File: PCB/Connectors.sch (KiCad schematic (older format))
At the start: 18 parts

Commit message: Switch 3.3V analog circuitry to low noise supply, fix pin classifications on some parts, swap 9V connector for 10V
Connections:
- net labels added: +10V
- net labels removed: +9V
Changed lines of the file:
@@
 Wire Wire Line
 	6300 4550 6200 4550
-$Comp
-L power:+9V #PWR?
-U 1 1 5DEFE9A9
-P 6200 4550
-F 0 "#PWR?" H 6200 4400 50  0001 C CNN
-F 1 "+9V" H 6215 4723 50  0000 C CNN
-F 2 "" H 6200 4550 50  0001 C CNN
-F 3 "" H 6200 4550 50  0001 C CNN
-	1    6200 4550
-	1    0    0    -1
-$EndComp
 Text GLabel 4800 6250 0    50   Input ~ 0
 FPGA-CS
@@
 Wire Wire Line
 	3550 2000 3650 2000
+$Comp
+L power:+10V #PWR?
+U 1 1 5E281EB9
+P 6200 4550
+F 0 "#PWR?" H 6200 4400 50  0001 C CNN
+F 1 "+10V" H 6215 4723 50  0000 C CNN
+F 2 "" H 6200 4550 50  0001 C CNN
+F 3 "" H 6200 4550 50  0001 C CNN
+	1    6200 4550
+	1    0    0    -1
+$EndComp
 $EndSCHEMATC

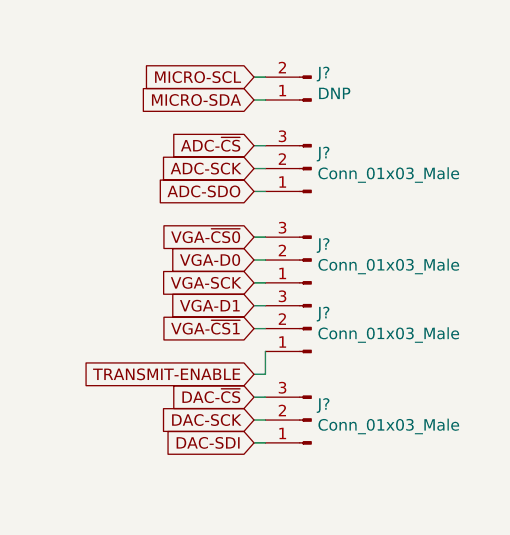
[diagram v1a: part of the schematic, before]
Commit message: Add missing footprints
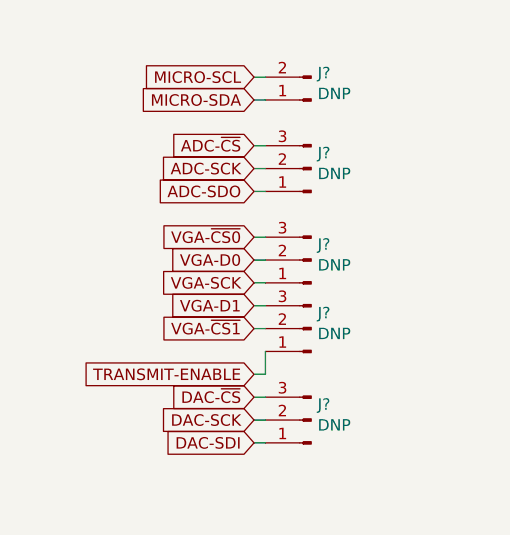
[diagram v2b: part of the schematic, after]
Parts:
- H? (x2): footprint (none) -> Mounting_Holes:MountingHole_4mm_Pad_Via
- J? (x4): value Conn_01x03_Male -> DNP; footprint (none) -> Pin_Headers:Pin_Header_Straight_1x03_Pitch2.54mm
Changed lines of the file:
@@
 P 9050 4900
 F 0 "J?" H 9022 4832 50  0000 R CNN
-F 1 "Conn_01x03_Male" H 9022 4923 50  0000 R CNN
-F 2 "" H 9050 4900 50  0001 C CNN
+F 1 "DNP" H 9022 4923 50  0000 R CNN
+F 2 "Pin_Headers:Pin_Header_Straight_1x03_Pitch2.54mm" H 9050 4900 50  0001 C CNN
 F 3 "~" H 9050 4900 50  0001 C CNN
 	1    9050 4900
@@
 P 9050 5300
 F 0 "J?" H 9022 5232 50  0000 R CNN
-F 1 "Conn_01x03_Male" H 9022 5323 50  0000 R CNN
-F 2 "" H 9050 5300 50  0001 C CNN
+F 1 "DNP" H 9022 5323 50  0000 R CNN
+F 2 "Pin_Headers:Pin_Header_Straight_1x03_Pitch2.54mm" H 9050 5300 50  0001 C CNN
 F 3 "~" H 9050 5300 50  0001 C CNN
 	1    9050 5300
@@
 P 9050 5600
 F 0 "J?" H 9022 5532 50  0000 R CNN
-F 1 "Conn_01x03_Male" H 9022 5623 50  0000 R CNN
-F 2 "" H 9050 5600 50  0001 C CNN
+F 1 "DNP" H 9022 5623 50  0000 R CNN
+F 2 "Pin_Headers:Pin_Header_Straight_1x03_Pitch2.54mm" H 9050 5600 50  0001 C CNN
 F 3 "~" H 9050 5600 50  0001 C CNN
 	1    9050 5600
@@
 P 9050 6000
 F 0 "J?" H 9022 5932 50  0000 R CNN
-F 1 "Conn_01x03_Male" H 9022 6023 50  0000 R CNN
-F 2 "" H 9050 6000 50  0001 C CNN
+F 1 "DNP" H 9022 6023 50  0000 R CNN
+F 2 "Pin_Headers:Pin_Header_Straight_1x03_Pitch2.54mm" H 9050 6000 50  0001 C CNN
 F 3 "~" H 9050 6000 50  0001 C CNN
 	1    9050 6000
@@
 F 0 "H?" V 3704 2400 50  0000 L CNN
 F 1 "MountingHole_Pad" V 3795 2400 50  0000 L CNN
-F 2 "" H 3750 2250 50  0001 C CNN
+F 2 "Mounting_Holes:MountingHole_4mm_Pad_Via" H 3750 2250 50  0001 C CNN
 F 3 "~" H 3750 2250 50  0001 C CNN
 	1    3750 2250
@@
 F 0 "H?" V 3704 2150 50  0000 L CNN
 F 1 "MountingHole_Pad" V 3795 2150 50  0000 L CNN
-F 2 "" H 3750 2000 50  0001 C CNN
+F 2 "Mounting_Holes:MountingHole_4mm_Pad_Via" H 3750 2000 50  0001 C CNN
 F 3 "~" H 3750 2000 50  0001 C CNN
 	1    3750 2000

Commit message: Annotate schematic, simplify transmit circuit, shuffle receive opamp stages, reorder buttons so they match net names, reorder connectors to simplify routing, begin arranging parts on PCB
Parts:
- gave numbers to parts that had none: 18
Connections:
- net ADC-SCK: now also J8.1 (Pin_1); no longer J8.2 (Pin_2)
- net ADC-SDO: now also J8.2 (Pin_2); no longer J8.1 (Pin_1)
- net DAC-SCK: now also J15.1 (Pin_1); no longer J15.2 (Pin_2)
- net DAC-SDI: now also J15.2 (Pin_2); no longer J15.1 (Pin_1)

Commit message: Begin layout around FPGA and microcontroller, rearrange some connections to FPGA and microcontroller, change groupings of optional debug pins
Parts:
- removed J10, J11, J15: DNP, Pin_Headers:Pin_Header_Straight_1x03_Pitch2.54mm, symbol Connector:Conn_01x03_Male
- removed J12: PH1-08-UA, Pin_Headers:Pin_Header_Straight_1x08_Pitch2.54mm, symbol Connector:Conn_01x08_Male
- added J10: DNP, Pin_Headers:Pin_Header_Straight_1x05_Pitch2.54mm, symbol Connector:Conn_01x05_Male
- added J11: DNP, Pin_Headers:Pin_Header_Straight_2x05_Pitch2.54mm, symbol Connector_Generic:Conn_02x05_Odd_Even
- added J14: DNP, Pin_Headers:Pin_Header_Straight_1x04_Pitch2.54mm, symbol Connector:Conn_01x04_Male
- renumbered J13 to J12, J14 to J13
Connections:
- net +2V5: now also J11.4 (Pin_4)
- net DAC-SCK: now also J14.3 (Pin_3)
- net DAC-SDI: now also J14.2 (Pin_2)
- net DAC-~CS: now also J14.1 (Pin_1)
- net FPGA-TCK: now also J11.1 (Pin_1)
- net FPGA-TDI: now also J11.9 (Pin_9)
- net FPGA-TDO: now also J11.3 (Pin_3)
- net FPGA-TMS: now also J11.5 (Pin_5)
- net GND: now also J11.10 (Pin_10), J11.2 (Pin_2)
- net TRANSMIT-ENABLE: now also J14.4 (Pin_4)
- net VGA-D0: now also J10.2 (Pin_2)
- net VGA-D1: now also J10.5 (Pin_5)
- net VGA-SCK: now also J10.3 (Pin_3)
- net VGA-~CS0: now also J10.1 (Pin_1)
- net VGA-~CS1: now also J10.4 (Pin_4)
- no-connect marks 0 -> 3
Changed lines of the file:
@@
 Wire Wire Line
 	5700 3000 5700 3050
-Text GLabel 2750 5850 0    50   Input ~ 0
+Text GLabel 2500 5950 0    50   Input ~ 0
 FPGA-TDI
-Text GLabel 2750 5650 0    50   Input ~ 0
+Text GLabel 2500 5550 0    50   Input ~ 0
 FPGA-TCK
-Text GLabel 2750 5950 0    50   Input ~ 0
+Text GLabel 2500 5750 0    50   Input ~ 0
 FPGA-TMS
-Text GLabel 2750 6050 0    50   Input ~ 0
+Text GLabel 2500 5650 0    50   Input ~ 0
 FPGA-TDO
 $Comp
@@
 Wire Wire Line
 	2750 4300 2800 4300
-$Comp
-L Connector:Conn_01x08_Male J12
-U 1 1 5DD1A649
-P 3000 5850
-F 0 "J12" H 2972 5824 50  0000 R CNN
-F 1 "PH1-08-UA" H 2972 5733 50  0000 R CNN
-F 2 "Pin_Headers:Pin_Header_Straight_1x08_Pitch2.54mm" H 3000 5850 50  0001 C CNN
-F 3 "https://www.digikey.ca/product-detail/en/adam-tech/PH1-08-UA/2057-PH1-08-UA-ND/9830442" H 3000 5850 50  0001 C CNN
-	1    3000 5850
-	-1   0    0    -1
-$EndComp
 Wire Wire Line
 	2750 4500 2800 4500
@@
 	2050 4100 2800 4100
 Connection ~ 2050 4400
-Wire Wire Line
-	2700 5550 2800 5550
 $Comp
 L power:GND #PWR0194
 U 1 1 5DD3A2BB
-P 2050 6200
-F 0 "#PWR0194" H 2050 5950 50  0001 C CNN
-F 1 "GND" H 2055 6027 50  0000 C CNN
-F 2 "" H 2050 6200 50  0001 C CNN
-F 3 "" H 2050 6200 50  0001 C CNN
-	1    2050 6200
-	1    0    0    -1
-$EndComp
-Wire Wire Line
-	2750 5650 2800 5650
-Wire Wire Line
-	2750 6050 2800 6050
-Wire Wire Line
-	2800 5950 2750 5950
-Wire Wire Line
-	2750 5850 2800 5850
-Wire Wire Line
-	2050 6200 2050 6150
-Wire Wire Line
-	2050 6150 2800 6150
-Wire Wire Line
-	2050 6150 2050 5750
-Wire Wire Line
-	2050 5750 2800 5750
-Connection ~ 2050 6150
+P 3150 6000
+F 0 "#PWR0194" H 3150 5750 50  0001 C CNN
+F 1 "GND" H 3155 5827 50  0000 C CNN
+F 2 "" H 3150 6000 50  0001 C CNN
+F 3 "" H 3150 6000 50  0001 C CNN
+	1    3150 6000
+	1    0    0    -1
+$EndComp
 $Comp
 L Connector:Conn_01x02_Male J2
@@
 L power:+2V5 #PWR0191
 U 1 1 5DDAEE31
-P 2700 5550
-F 0 "#PWR0191" H 2700 5400 50  0001 C CNN
-F 1 "+2V5" H 2715 5723 50  0000 C CNN
-F 2 "" H 2700 5550 50  0001 C CNN
-F 3 "" H 2700 5550 50  0001 C CNN
-	1    2700 5550
+P 3250 5650
+F 0 "#PWR0191" H 3250 5500 50  0001 C CNN
+F 1 "+2V5" H 3265 5823 50  0000 C CNN
+F 2 "" H 3250 5650 50  0001 C CNN
+F 3 "" H 3250 5650 50  0001 C CNN
+	1    3250 5650
 	1    0    0    -1
 $EndComp
@@
 $EndComp
 $Comp
-L Connector:Conn_01x02_Male J14
+L Connector:Conn_01x02_Male J13
 U 1 1 5DED5F02
 P 6500 5950
-F 0 "J14" H 6472 5832 50  0000 R CNN
+F 0 "J13" H 6472 5832 50  0000 R CNN
 F 1 "DNP" H 6472 5923 50  0000 R CNN
 F 2 "Pin_Headers:Pin_Header_Straight_1x02_Pitch2.54mm" H 6500 5950 50  0001 C CNN
@@
 $EndComp
 $Comp
-L Connector:Conn_01x08_Male J13
+L Connector:Conn_01x08_Male J12
 U 1 1 5DEE094B
 P 5050 5850
-F 0 "J13" H 5022 5824 50  0000 R CNN
+F 0 "J12" H 5022 5824 50  0000 R CNN
 F 1 "DNP" H 5022 5733 50  0000 R CNN
 F 2 "Pin_Headers:Pin_Header_Straight_1x08_Pitch2.54mm" H 5050 5850 50  0001 C CNN
@@
 Text GLabel 8800 4900 0    50   Input ~ 0
 ADC-SDO
-Text GLabel 8800 5200 0    50   Input ~ 0
+Text GLabel 8800 5600 0    50   Input ~ 0
 VGA-~CS0
-Text GLabel 8800 5300 0    50   Input ~ 0
+Text GLabel 8800 5500 0    50   Input ~ 0
 VGA-D0
 Text GLabel 8800 5400 0    50   Input ~ 0
 VGA-SCK
-Text GLabel 8800 5500 0    50   Input ~ 0
+Text GLabel 8800 5200 0    50   Input ~ 0
 VGA-D1
-Text GLabel 8800 5600 0    50   Input ~ 0
+Text GLabel 8800 5300 0    50   Input ~ 0
 VGA-~CS1
+Text GLabel 8800 6100 0    50   Input ~ 0
+DAC-~CS
 Text GLabel 8800 5900 0    50   Input ~ 0
-DAC-~CS
-Text GLabel 8800 6100 0    50   Input ~ 0
 DAC-SCK
 Text GLabel 8800 6000 0    50   Input ~ 0
@@
 Wire Wire Line
 	8800 5000 8850 5000
-$Comp
-L Connector:Conn_01x03_Male J10
-U 1 1 5E232910
-P 9050 5300
-F 0 "J10" H 9022 5232 50  0000 R CNN
-F 1 "DNP" H 9022 5323 50  0000 R CNN
-F 2 "Pin_Headers:Pin_Header_Straight_1x03_Pitch2.54mm" H 9050 5300 50  0001 C CNN
-F 3 "~" H 9050 5300 50  0001 C CNN
-	1    9050 5300
-	-1   0    0    1
-$EndComp
 Wire Wire Line
 	8800 5200 8850 5200
@@
 Wire Wire Line
 	8800 5400 8850 5400
-$Comp
-L Connector:Conn_01x03_Male J11
-U 1 1 5E236FC5
-P 9050 5600
-F 0 "J11" H 9022 5532 50  0000 R CNN
-F 1 "DNP" H 9022 5623 50  0000 R CNN
-F 2 "Pin_Headers:Pin_Header_Straight_1x03_Pitch2.54mm" H 9050 5600 50  0001 C CNN
-F 3 "~" H 9050 5600 50  0001 C CNN
-	1    9050 5600
-	-1   0    0    1
-$EndComp
 Wire Wire Line
 	8800 5500 8850 5500
@@
 Wire Wire Line
 	8800 5800 8850 5800
-Wire Wire Line
-	8850 5800 8850 5700
-$Comp
-L Connector:Conn_01x03_Male J15
-U 1 1 5E23BCC1
-P 9050 6000
-F 0 "J15" H 9022 5932 50  0000 R CNN
-F 1 "DNP" H 9022 6023 50  0000 R CNN
-F 2 "Pin_Headers:Pin_Header_Straight_1x03_Pitch2.54mm" H 9050 6000 50  0001 C CNN
-F 3 "~" H 9050 6000 50  0001 C CNN
-	1    9050 6000
-	-1   0    0    1
-$EndComp
 Wire Wire Line
 	8800 5900 8850 5900
@@
 	1    0    0    -1
 $EndComp
+$Comp
+L Connector_Generic:Conn_02x05_Odd_Even J11
+U 1 1 5E09FA0E
+P 2750 5750
+F 0 "J11" H 2800 6167 50  0000 C CNN
+F 1 "DNP" H 2800 6076 50  0000 C CNN
+F 2 "Pin_Headers:Pin_Header_Straight_2x05_Pitch2.54mm" H 2750 5750 50  0001 C CNN
+F 3 "https://www.digikey.ca/product-detail/en/adam-tech/PH2-10-UA/2057-PH2-10-UA-ND/9830654" H 2750 5750 50  0001 C CNN
+	1    2750 5750
+	1    0    0    -1
+$EndComp
+Wire Wire Line
+	2500 5550 2550 5550
+Wire Wire Line
+	2500 5650 2550 5650
+Wire Wire Line
+	2500 5750 2550 5750
+Wire Wire Line
+	2500 5950 2550 5950
+Wire Wire Line
+	3050 5950 3150 5950
+Wire Wire Line
+	3150 5950 3150 6000
+Wire Wire Line
+	3050 5550 3150 5550
+Wire Wire Line
+	3150 5550 3150 5950
+Connection ~ 3150 5950
+Wire Wire Line
+	3050 5650 3250 5650
+NoConn ~ 3050 5750
+NoConn ~ 3050 5850
+NoConn ~ 2550 5850
+$Comp
+L Connector:Conn_01x04_Male J14
+U 1 1 5E5FD68B
+P 9050 6000
+F 0 "J14" H 9022 5882 50  0000 R CNN
+F 1 "DNP" H 9022 5973 50  0000 R CNN
+F 2 "Pin_Headers:Pin_Header_Straight_1x04_Pitch2.54mm" H 9050 6000 50  0001 C CNN
+F 3 "~" H 9050 6000 50  0001 C CNN
+	1    9050 6000
+	-1   0    0    1
+$EndComp
+$Comp
+L Connector:Conn_01x05_Male J10
+U 1 1 5E600171
+P 9050 5400
+F 0 "J10" H 9022 5332 50  0000 R CNN
+F 1 "DNP" H 9022 5423 50  0000 R CNN
+F 2 "Pin_Headers:Pin_Header_Straight_1x05_Pitch2.54mm" H 9050 5400 50  0001 C CNN
+F 3 "~" H 9050 5400 50  0001 C CNN
+	1    9050 5400
+	-1   0    0    1
+$EndComp
 $EndSCHEMATC

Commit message: Remove unnecessary series resistors, rearrange connections on FPGA and microcontroller, rearrange debug pins, layout most of FPGA and microcontroller sections
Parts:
- removed J12, J5: DNP, Pin_Headers:Pin_Header_Straight_1x08_Pitch2.54mm, symbol Connector:Conn_01x08_Male
- added J5: DNP, Pin_Headers:Pin_Header_Straight_1x15_Pitch2.54mm, symbol Connector:Conn_01x15_Male
- renumbered J13 to J12, J14 to J13, R68 to R64
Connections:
- net FPGA-CONF_DONE: now also J5.1 (Pin_1)
- net FPGA-CRC_ERROR: now also J5.3 (Pin_3)
- net FPGA-CS: now also J5.11 (Pin_11)
- net FPGA-DCLK: now also J5.13 (Pin_13)
- net FPGA-DIN: now also J5.14 (Pin_14)
- net FPGA-DOUT: now also J5.12 (Pin_12)
- net FPGA-INIT_DONE: now also J5.2 (Pin_2)
- net FPGA-LINK0: now also J5.4 (Pin_4)
- net FPGA-LINK1: now also J5.5 (Pin_5)
- net FPGA-LINK2: now also J5.6 (Pin_6)
- net FPGA-LINK3: now also J5.7 (Pin_7)
- net FPGA-LINK4: now also J5.8 (Pin_8)
- net FPGA-LINK5: now also J5.9 (Pin_9)
- net FPGA-nCONFIG: now also J5.15 (Pin_15)
- net FPGA-nSTATUS: now also J5.10 (Pin_10)
- net MICRO-SCL: now also J6.1 (Pin_1); no longer J6.2 (Pin_2)
- net MICRO-SDA: now also J6.2 (Pin_2); no longer J6.1 (Pin_1)
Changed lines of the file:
@@
 $EndDescr
 $Comp
-L power:GND #PWR0180
+L power:GND #PWR0179
 U 1 1 5DCE40E5
 P 2750 2200
-F 0 "#PWR0180" H 2750 1950 50  0001 C CNN
+F 0 "#PWR0179" H 2750 1950 50  0001 C CNN
 F 1 "GND" H 2755 2027 50  0000 C CNN
 F 2 "" H 2750 2200 50  0001 C CNN
@@
 $EndComp
 $Comp
-L power:+BATT #PWR0178
+L power:+BATT #PWR0177
 U 1 1 5DCED91D
 P 3000 2000
-F 0 "#PWR0178" H 3000 1850 50  0001 C CNN
+F 0 "#PWR0177" H 3000 1850 50  0001 C CNN
 F 1 "+BATT" H 3015 2173 50  0000 C CNN
 F 2 "" H 3000 2000 50  0001 C CNN
@@
 TRANSDUCER
 $Comp
-L Device:R R68
+L Device:R R64
 U 1 1 5DE80022
 P 5700 2800
-F 0 "R68" H 5770 2846 50  0000 L CNN
+F 0 "R64" H 5770 2846 50  0000 L CNN
 F 1 "10k" H 5770 2755 50  0000 L CNN
 F 2 "Resistors_SMD:R_1206_HandSoldering" V 5630 2800 50  0001 C CNN
@@
 	5700 2550 5700 2650
 $Comp
-L power:GND #PWR0182
+L power:GND #PWR0181
 U 1 1 5DE80E0C
 P 5700 3050
-F 0 "#PWR0182" H 5700 2800 50  0001 C CNN
+F 0 "#PWR0181" H 5700 2800 50  0001 C CNN
 F 1 "GND" H 5705 2877 50  0000 C CNN
 F 2 "" H 5700 3050 50  0001 C CNN
@@
 FPGA-TDO
 $Comp
-L power:+3V3 #PWR0183
+L power:+3V3 #PWR0182
 U 1 1 5DED008E
 P 2700 3900
-F 0 "#PWR0183" H 2700 3750 50  0001 C CNN
+F 0 "#PWR0182" H 2700 3750 50  0001 C CNN
 F 1 "+3V3" H 2715 4073 50  0000 C CNN
 F 2 "" H 2700 3900 50  0001 C CNN
@@
 	2800 4600 2750 4600
 $Comp
-L power:GND #PWR0186
+L power:GND #PWR0185
 U 1 1 5DD2AB1C
 P 2050 4450
-F 0 "#PWR0186" H 2050 4200 50  0001 C CNN
+F 0 "#PWR0185" H 2050 4200 50  0001 C CNN
 F 1 "GND" H 2055 4277 50  0000 C CNN
 F 2 "" H 2050 4450 50  0001 C CNN
@@
 Connection ~ 2050 4400
 $Comp
-L power:GND #PWR0194
+L power:GND #PWR0193
 U 1 1 5DD3A2BB
 P 3150 6000
-F 0 "#PWR0194" H 3150 5750 50  0001 C CNN
+F 0 "#PWR0193" H 3150 5750 50  0001 C CNN
 F 1 "GND" H 3155 5827 50  0000 C CNN
 F 2 "" H 3150 6000 50  0001 C CNN
@@
 	5950 2650 5950 3000
 $Comp
-L power:+2V5 #PWR0191
+L power:+2V5 #PWR0190
 U 1 1 5DDAEE31
 P 3250 5650
-F 0 "#PWR0191" H 3250 5500 50  0001 C CNN
+F 0 "#PWR0190" H 3250 5500 50  0001 C CNN
 F 1 "+2V5" H 3265 5823 50  0000 C CNN
 F 2 "" H 3250 5650 50  0001 C CNN
@@
 	1    0    0    -1
 $EndComp
-$Comp
-L Connector:Conn_01x08_Male J5
-U 1 1 5DF84ABE
-P 5050 4200
-F 0 "J5" H 5022 4174 50  0000 R CNN
-F 1 "DNP" H 5022 4083 50  0000 R CNN
-F 2 "Pin_Headers:Pin_Header_Straight_1x08_Pitch2.54mm" H 5050 4200 50  0001 C CNN
-F 3 "https://www.digikey.ca/product-detail/en/adam-tech/PH1-08-UA/2057-PH1-08-UA-ND/9830442" H 5050 4200 50  0001 C CNN
-	1    5050 4200
-	-1   0    0    -1
-$EndComp
+Text GLabel 4800 5000 0    50   Input ~ 0
+FPGA-DOUT
+Text GLabel 4800 4800 0    50   Input ~ 0
+FPGA-nSTATUS
+Text GLabel 4800 5100 0    50   Input ~ 0
+FPGA-DCLK
+Text GLabel 4800 5200 0    50   Input ~ 0
+FPGA-DIN
+Text GLabel 4800 5300 0    50   Input ~ 0
+FPGA-nCONFIG
 Text GLabel 4800 3900 0    50   Input ~ 0
-FPGA-DOUT
-Text GLabel 4800 4400 0    50   Input ~ 0
-FPGA-nSTATUS
+FPGA-CONF_DONE
 Text GLabel 4800 4000 0    50   Input ~ 0
-FPGA-DCLK
+FPGA-INIT_DONE
 Text GLabel 4800 4100 0    50   Input ~ 0
-FPGA-DIN
-Text GLabel 4800 4500 0    50   Input ~ 0
-FPGA-nCONFIG
-Text GLabel 4800 4200 0    50   Input ~ 0
-FPGA-CONF_DONE
-Text GLabel 4800 4600 0    50   Input ~ 0
-FPGA-INIT_DONE
-Text GLabel 4800 4300 0    50   Input ~ 0
 FPGA-CRC_ERROR
 Wire Wire Line
@@
 $EndComp
 $Comp
-L power:+1V2 #PWR0184
+L power:+1V2 #PWR0183
 U 1 1 5DECE3B1
 P 6200 3900
-F 0 "#PWR0184" H 6200 3750 50  0001 C CNN
+F 0 "#PWR0183" H 6200 3750 50  0001 C CNN
 F 1 "+1V2" H 6215 4073 50  0000 C CNN
 F 2 "" H 6200 3900 50  0001 C CNN
@@
 	6200 3900 6300 3900
 $Comp
-L power:GND #PWR0185
+L power:GND #PWR0184
 U 1 1 5DECF8CC
 P 6200 4000
-F 0 "#PWR0185" H 6200 3750 50  0001 C CNN
+F 0 "#PWR0184" H 6200 3750 50  0001 C CNN
 F 1 "GND" H 6205 3827 50  0000 C CNN
 F 2 "" H 6200 4000 50  0001 C CNN
@@
 	6200 5200 6300 5200
 $Comp
-L power:GND #PWR0190
+L power:GND #PWR0189
 U 1 1 5DED29DD
 P 6200 5300
-F 0 "#PWR0190" H 6200 5050 50  0001 C CNN
+F 0 "#PWR0189" H 6200 5050 50  0001 C CNN
 F 1 "GND" H 6205 5127 50  0000 C CNN
 F 2 "" H 6200 5300 50  0001 C CNN
@@
 	6200 5300 6300 5300
 $Comp
-L power:+12V #PWR0189
+L power:+12V #PWR0188
 U 1 1 5DED51C9
 P 6200 5200
-F 0 "#PWR0189" H 6200 5050 50  0001 C CNN
+F 0 "#PWR0188" H 6200 5050 50  0001 C CNN
 F 1 "+12V" H 6215 5373 50  0000 C CNN
 F 2 "" H 6200 5200 50  0001 C CNN
@@
 $EndComp
 $Comp
-L Connector:Conn_01x02_Male J13
+L Connector:Conn_01x02_Male J12
 U 1 1 5DED5F02
 P 6500 5950
-F 0 "J13" H 6472 5832 50  0000 R CNN
+F 0 "J12" H 6472 5832 50  0000 R CNN
 F 1 "DNP" H 6472 5923 50  0000 R CNN
 F 2 "Pin_Headers:Pin_Header_Straight_1x02_Pitch2.54mm" H 6500 5950 50  0001 C CNN
@@
 	6200 5850 6300 5850
 $Comp
-L power:GND #PWR0193
+L power:GND #PWR0192
 U 1 1 5DED5F0D
 P 6200 5950
-F 0 "#PWR0193" H 6200 5700 50  0001 C CNN
+F 0 "#PWR0192" H 6200 5700 50  0001 C CNN
 F 1 "GND" H 6205 5777 50  0000 C CNN
 F 2 "" H 6200 5950 50  0001 C CNN
@@
 	6200 5950 6300 5950
 $Comp
-L Parts:+50V #PWR0192
+L Parts:+50V #PWR0191
 U 1 1 5DED7ED3
 P 6200 5850
-F 0 "#PWR0192" H 6200 5700 50  0001 C CNN
+F 0 "#PWR0191" H 6200 5700 50  0001 C CNN
 F 1 "+50V" H 6215 6023 50  0000 C CNN
 F 2 "" H 6200 5850 50  0001 C CNN
@@
 	1    0    0    -1
 $EndComp
-$Comp
-L Connector:Conn_01x08_Male J12
-U 1 1 5DEE094B
-P 5050 5850
-F 0 "J12" H 5022 5824 50  0000 R CNN
-F 1 "DNP" H 5022 5733 50  0000 R CNN
-F 2 "Pin_Headers:Pin_Header_Straight_1x08_Pitch2.54mm" H 5050 5850 50  0001 C CNN
-F 3 "https://www.digikey.ca/product-detail/en/adam-tech/PH1-08-UA/2057-PH1-08-UA-ND/9830442" H 5050 5850 50  0001 C CNN
-	1    5050 5850
-	-1   0    0    -1
-$EndComp
-Text GLabel 4800 5550 0    50   Input ~ 0
+Text GLabel 4800 4200 0    50   Input ~ 0
 FPGA-LINK0
-Text GLabel 4800 5650 0    50   Input ~ 0
+Text GLabel 4800 4300 0    50   Input ~ 0
 FPGA-LINK1
-Text GLabel 4800 5750 0    50   Input ~ 0
+Text GLabel 4800 4400 0    50   Input ~ 0
 FPGA-LINK2
-Text GLabel 4800 5850 0    50   Input ~ 0
+Text GLabel 4800 4500 0    50   Input ~ 0
 FPGA-LINK3
-Text GLabel 4800 5950 0    50   Input ~ 0
+Text GLabel 4800 4600 0    50   Input ~ 0
 FPGA-LINK4
-Text GLabel 4800 6050 0    50   Input ~ 0
+Text GLabel 4800 4700 0    50   Input ~ 0
 FPGA-LINK5
 Wire Wire Line
-	4800 5550 4850 5550
-Wire Wire Line
-	4850 5650 4800 5650
-Wire Wire Line
-	4800 5750 4850 5750
-Wire Wire Line
-	4800 5850 4850 5850
-Wire Wire Line
-	4850 5950 4800 5950
-Wire Wire Line
-	4800 6050 4850 6050
+	4800 4700 4850 4700
+Wire Wire Line
+	4850 4800 4800 4800
+Wire Wire Line
+	4800 4900 4850 4900
+Wire Wire Line
+	4800 5000 4850 5000
+Wire Wire Line
+	4850 5100 4800 5100
+Wire Wire Line
+	4800 5200 4850 5200
 $Comp
 L Connector:Conn_01x02_Male J7
@@
 $EndComp
 $Comp
-L power:GND #PWR0188
+L power:GND #PWR0187
 U 1 1 5DEFAC45
 P 6200 4650
-F 0 "#PWR0188" H 6200 4400 50  0001 C CNN
+F 0 "#PWR0187" H 6200 4400 50  0001 C CNN
 F 1 "GND" H 6205 4477 50  0000 C CNN
 F 2 "" H 6200 4650 50  0001 C CNN
@@
 Wire Wire Line
 	6300 4550 6200 4550
-Text GLabel 4800 6250 0    50   Input ~ 0
+Text GLabel 4800 4900 0    50   Input ~ 0
 FPGA-CS
+Text GLabel 8800 4600 0    50   Input ~ 0
+MICRO-SCL
 Text GLabel 8800 4500 0    50   Input ~ 0
-MICRO-SCL
-Text GLabel 8800 4600 0    50   Input ~ 0
 MICRO-SDA
 Text GLabel 8800 4800 0    50   Input ~ 0
@@
 Text GLabel 8800 5800 0    50   Input ~ 0
 TRANSMIT-ENABLE
-Wire Wire Line
-	4800 6250 4850 6250
 $Comp
 L Connector:Conn_01x02_Male J6
@@
 $EndComp
 $Comp
-L power:GND #PWR0181
+L power:GND #PWR0180
 U 1 1 5E243B36
 P 3550 2250
-F 0 "#PWR0181" H 3550 2000 50  0001 C CNN
+F 0 "#PWR0180" H 3550 2000 50  0001 C CNN
 F 1 "GND" H 3555 2077 50  0000 C CNN
 F 2 "" H 3550 2250 50  0001 C CNN
@@
 $EndComp
 $Comp
-L power:+BATT #PWR0179
+L power:+BATT #PWR0178
 U 1 1 5E24725E
 P 3550 2000
-F 0 "#PWR0179" H 3550 1850 50  0001 C CNN
+F 0 "#PWR0178" H 3550 1850 50  0001 C CNN
 F 1 "+BATT" H 3565 2173 50  0000 C CNN
 F 2 "" H 3550 2000 50  0001 C CNN
@@
 	3550 2000 3650 2000
 $Comp
-L power:+10V #PWR0187
+L power:+10V #PWR0186
 U 1 1 5E281EB9
 P 6200 4550
-F 0 "#PWR0187" H 6200 4400 50  0001 C CNN
+F 0 "#PWR0186" H 6200 4400 50  0001 C CNN
 F 1 "+10V" H 6215 4723 50  0000 C CNN
 F 2 "" H 6200 4550 50  0001 C CNN
@@
 NoConn ~ 2550 5850
 $Comp
-L Connector:Conn_01x04_Male J14
+L Connector:Conn_01x04_Male J13
 U 1 1 5E5FD68B
 P 9050 6000
-F 0 "J14" H 9022 5882 50  0000 R CNN
+F 0 "J13" H 9022 5882 50  0000 R CNN
 F 1 "DNP" H 9022 5973 50  0000 R CNN
 F 2 "Pin_Headers:Pin_Header_Straight_1x04_Pitch2.54mm" H 9050 6000 50  0001 C CNN
@@
 	-1   0    0    1
 $EndComp
+Wire Wire Line
+	4850 5300 4800 5300
+$Comp
+L Connector:Conn_01x15_Male J5
+U 1 1 5E135391
+P 5050 4600
+F 0 "J5" H 5022 4624 50  0000 R CNN
+F 1 "DNP" H 5022 4533 50  0000 R CNN
+F 2 "Pin_Headers:Pin_Header_Straight_1x15_Pitch2.54mm" H 5050 4600 50  0001 C CNN
+F 3 "https://www.digikey.ca/product-detail/en/adam-tech/PH1-15-UA/2057-PH1-15-UA-ND/9830359" H 5050 4600 50  0001 C CNN
+	1    5050 4600
+	-1   0    0    -1
+$EndComp
 $EndSCHEMATC
